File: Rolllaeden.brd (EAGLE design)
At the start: 160 x 100 mm, 62 parts, among them IC1 PCF8574P, IC2 PCF8574P, IC3 74HCT04N, IC4 74HCT08N, IC5 74HCT08N, J1 J7MM, J2 J7MM, T1 BC337-25, T2 BC337-25, T3 BC337-25, T4 BC337-25, T5 BC337-25, T6 BC337-25

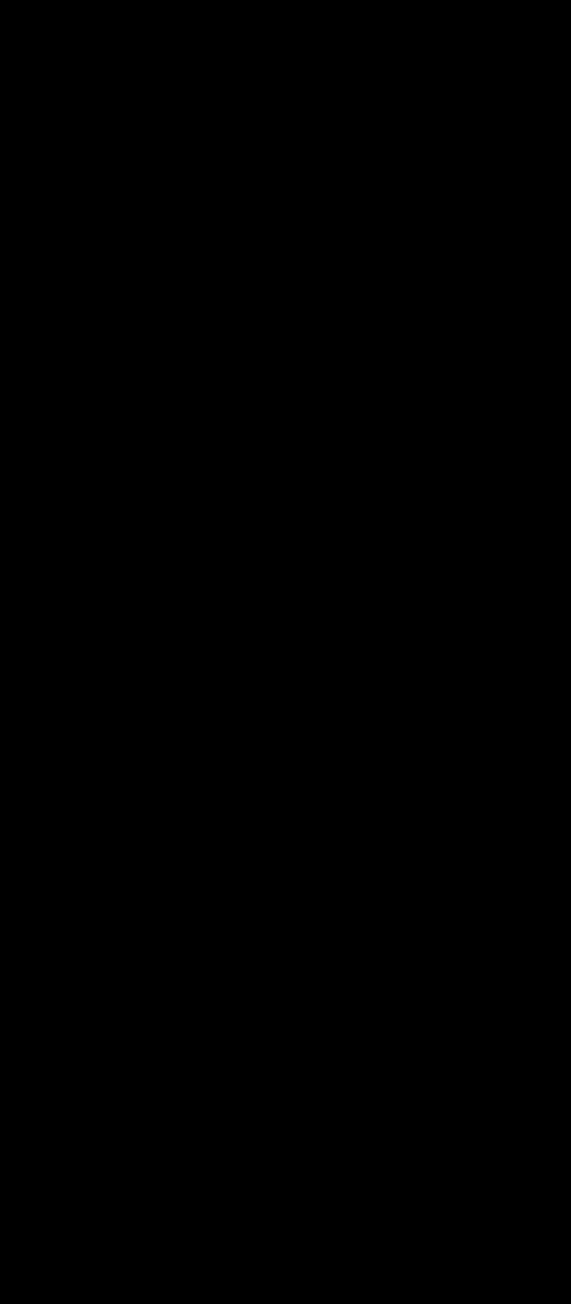
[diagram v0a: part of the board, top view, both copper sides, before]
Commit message: Pulldown-Widerstände zwichen Optokopplern und Logik-ICs hinzugefügt
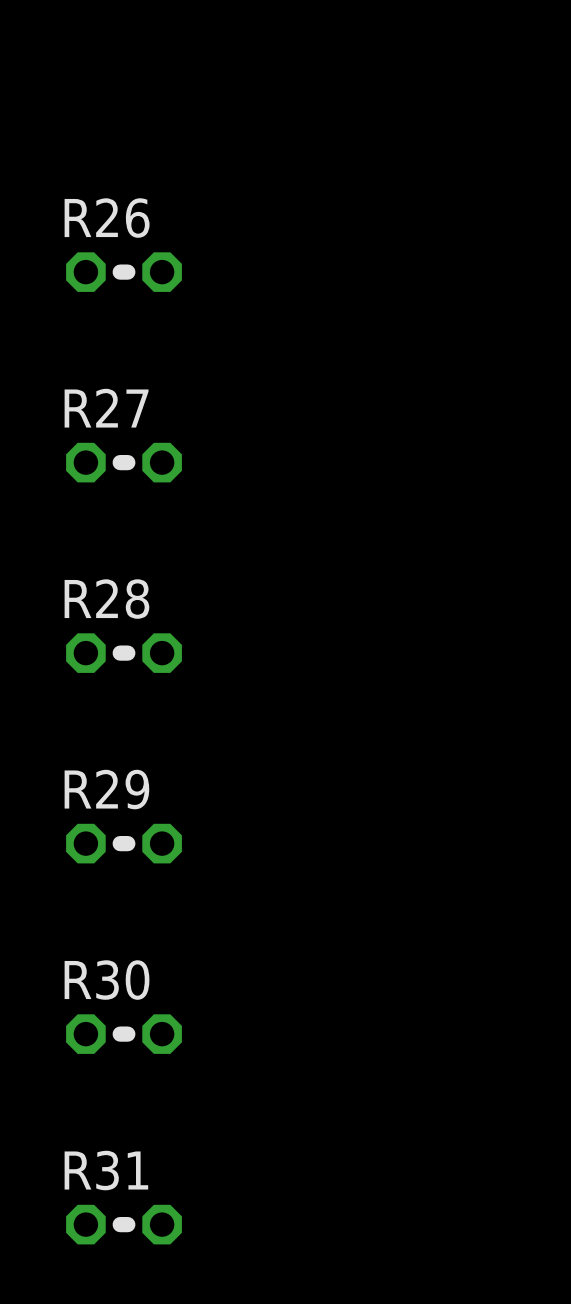
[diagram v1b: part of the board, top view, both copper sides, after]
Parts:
- added R26, R27, R28, R29, R30, R31: 10k, resistor:0204V
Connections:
- net GND: now also R26.1, R27.1, R28.1, R29.1, R30.1, R31.1
- net N$11: now also R30.2
- net N$22: now also R29.2
- net N$23: now also R28.2
- net N$34: now also R27.2
- net N$35: now also R26.2
- net N$4: now also R31.2
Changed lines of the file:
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@@
 <attribute name="OC_NEWARK" value="unknown" x="18.415" y="94.615" size="1.778" layer="27" display="off"/>
 </element>
+<element name="R26" library="resistor" package="0204V" value="10k" x="-11.43" y="-16.51"/>
+<element name="R27" library="resistor" package="0204V" value="10k" x="-11.43" y="-22.86"/>
+<element name="R28" library="resistor" package="0204V" value="10k" x="-11.43" y="-29.21"/>
+<element name="R29" library="resistor" package="0204V" value="10k" x="-11.43" y="-35.56"/>
+<element name="R30" library="resistor" package="0204V" value="10k" x="-11.43" y="-41.91"/>
+<element name="R31" library="resistor" package="0204V" value="10k" x="-11.43" y="-48.26"/>
 </elements>
 <signals>
@@
 <contactref element="SV3" pad="30T" route="any" routetag="1.30"/>
 <wire x1="5" y1="85.56" x2="9.36" y2="85.56" width="0.8128" layer="16"/>
+<contactref element="R26" pad="1"/>
+<contactref element="R27" pad="1"/>
+<contactref element="R28" pad="1"/>
+<contactref element="R29" pad="1"/>
+<contactref element="R30" pad="1"/>
+<contactref element="R31" pad="1"/>
+<wire x1="-12.7" y1="-41.91" x2="-12.7" y2="-48.26" width="0" layer="19" extent="1-1"/>
+<wire x1="-12.7" y1="-35.56" x2="-12.7" y2="-41.91" width="0" layer="19" extent="1-1"/>
+<wire x1="-12.7" y1="-29.21" x2="-12.7" y2="-35.56" width="0" layer="19" extent="1-1"/>
+<wire x1="-12.7" y1="-22.86" x2="-12.7" y2="-29.21" width="0" layer="19" extent="1-1"/>
+<wire x1="-12.7" y1="-16.51" x2="-12.7" y2="-22.86" width="0" layer="19" extent="1-1"/>
+<wire x1="46.99" y1="5.08" x2="-12.7" y2="-16.51" width="0" layer="19" extent="16-16"/>
 </signal>
 <signal name="N$1">
@@
 <wire x1="44.45" y1="54.61" x2="46.99" y2="57.15" width="0.4064" layer="1"/>
 <wire x1="46.99" y1="57.15" x2="49.53" y2="57.15" width="0.4064" layer="1"/>
+<contactref element="R31" pad="2"/>
+<wire x1="-10.16" y1="-48.26" x2="40.005" y2="37.465" width="0" layer="19" extent="1-1"/>
 </signal>
 <signal name="N$6">
@@
 <wire x1="50.8" y1="52.07" x2="49.53" y2="52.07" width="0.4064" layer="16"/>
 <wire x1="41.91" y1="39.37" x2="49.53" y2="39.37" width="0.4064" layer="1"/>
+<contactref element="R30" pad="2"/>
+<wire x1="-10.16" y1="-41.91" x2="41.91" y2="39.37" width="0" layer="19" extent="1-1"/>
 </signal>
 <signal name="N$16">
@@
 <wire x1="45.72" y1="27.94" x2="43.18" y2="30.48" width="0.4064" layer="1"/>
 <wire x1="43.18" y1="30.48" x2="41.91" y2="30.48" width="0.4064" layer="1"/>
+<contactref element="R29" pad="2"/>
+<wire x1="-10.16" y1="-35.56" x2="41.91" y2="30.48" width="0" layer="19" extent="1-1"/>
 </signal>
 <signal name="N$23">
@@
 <wire x1="39.37" y1="29.845" x2="40.005" y2="29.21" width="0.4064" layer="1"/>
 <wire x1="40.005" y1="29.21" x2="42.545" y2="29.21" width="0.4064" layer="1"/>
+<contactref element="R28" pad="2"/>
+<wire x1="-10.16" y1="-29.21" x2="41.91" y2="21.59" width="0" layer="19" extent="1-1"/>
 </signal>
 <signal name="N$25">
@@
 <wire x1="54.61" y1="10.16" x2="55.88" y2="8.89" width="0.4064" layer="16"/>
 <wire x1="55.88" y1="8.89" x2="57.15" y2="8.89" width="0.4064" layer="16"/>
+<contactref element="R27" pad="2"/>
+<wire x1="-10.16" y1="-22.86" x2="41.91" y2="12.7" width="0" layer="19" extent="1-1"/>
 </signal>
 <signal name="N$35">
@@
 <wire x1="44.45" y1="5.08" x2="43.18" y2="3.81" width="0.4064" layer="1"/>
 <wire x1="43.18" y1="3.81" x2="41.91" y2="3.81" width="0.4064" layer="1"/>
+<contactref element="R26" pad="2"/>
+<wire x1="-10.16" y1="-16.51" x2="41.91" y2="3.81" width="0" layer="19" extent="1-1"/>
 </signal>
 <signal name="N$36">

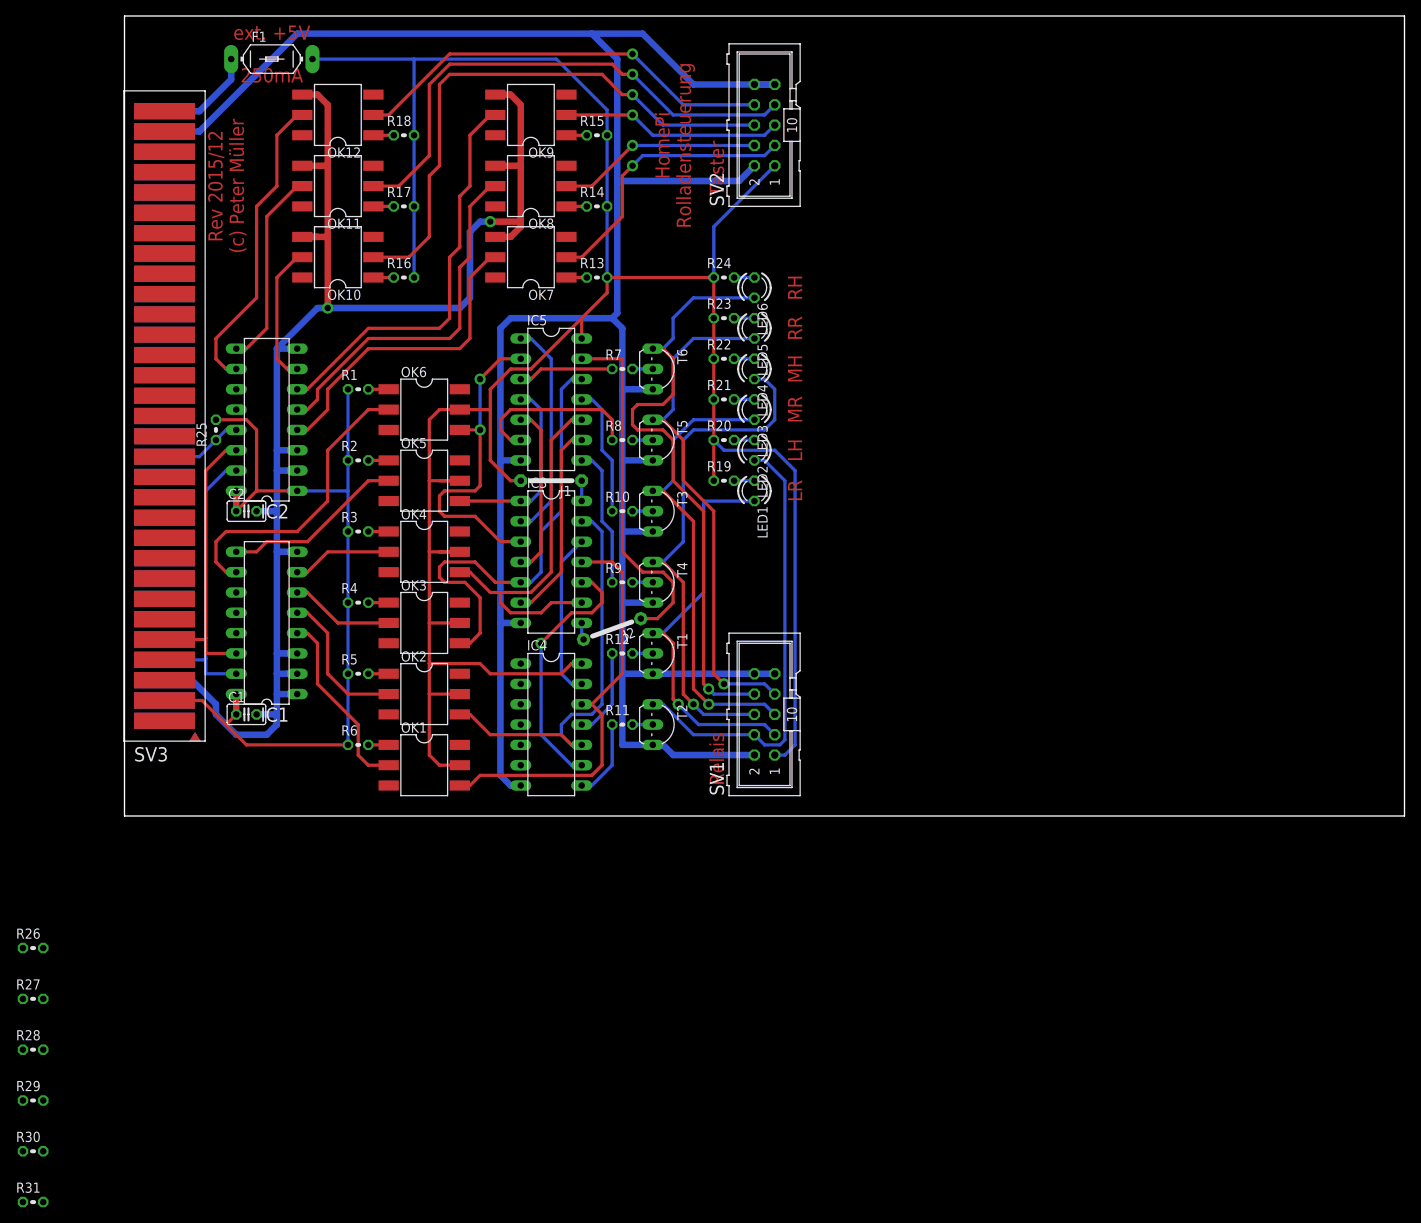
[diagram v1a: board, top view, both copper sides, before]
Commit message: Schaltpläne aufgehübscht zur Veröffentlichung
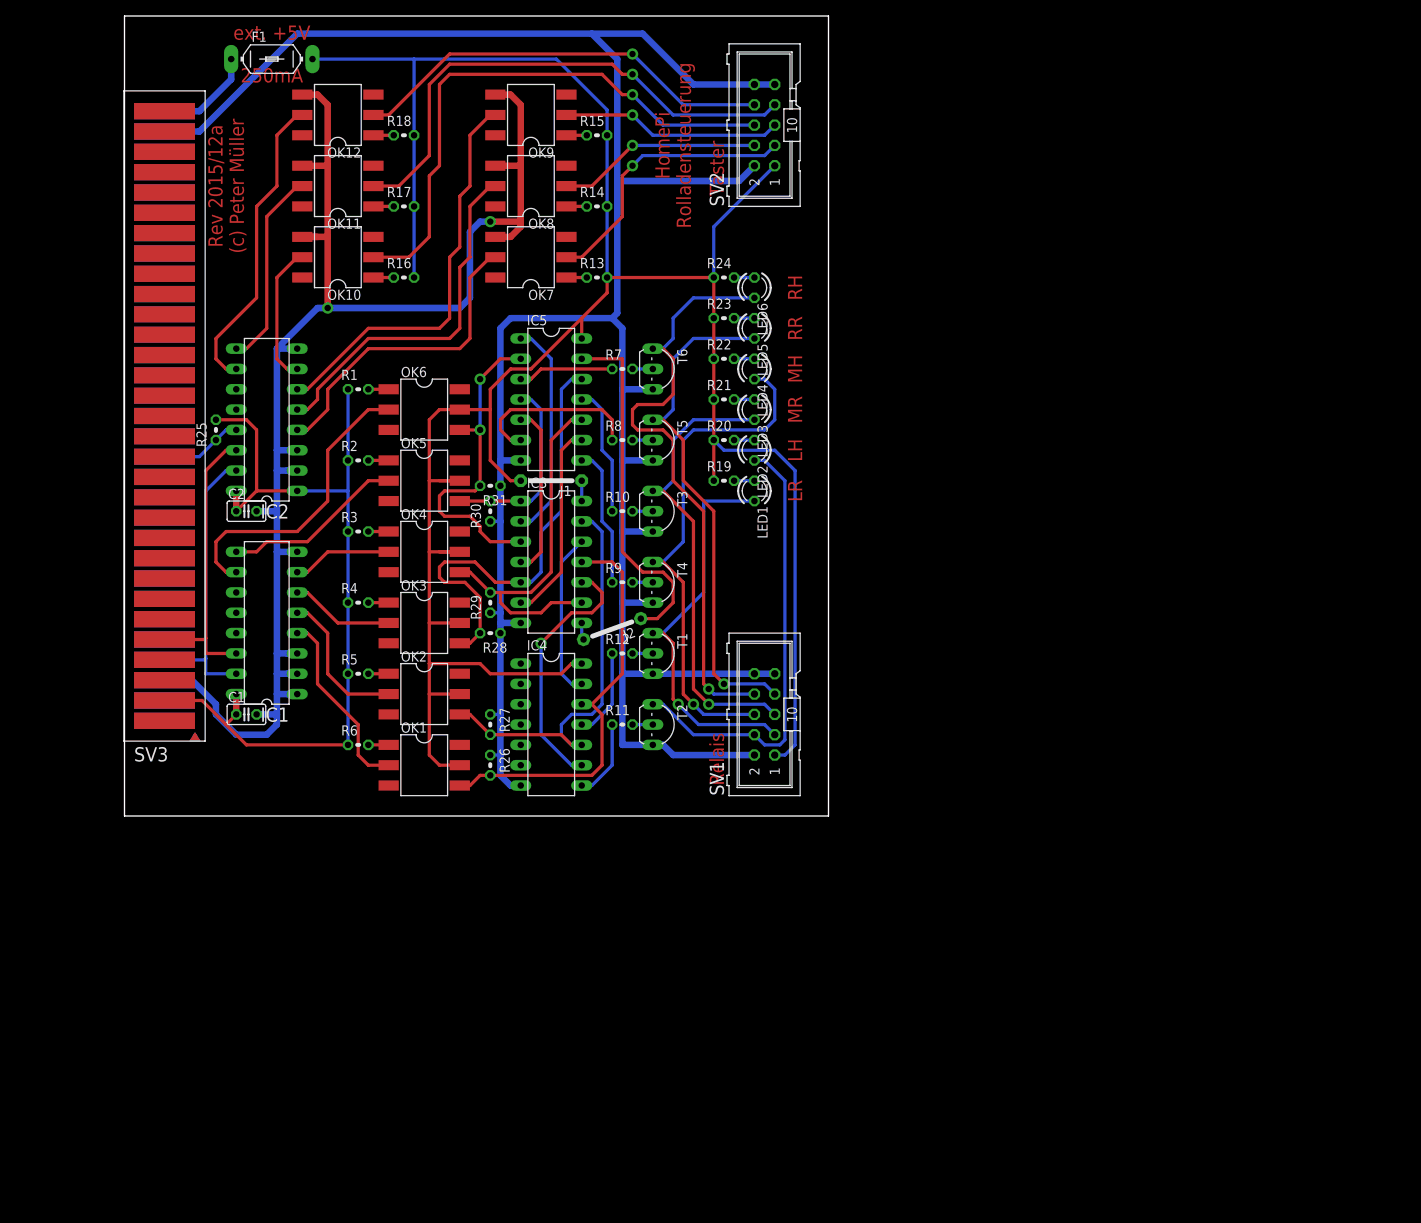
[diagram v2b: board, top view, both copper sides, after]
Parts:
- moved R31 106.2 mm to (45.7, 41.3), turned to 180 degrees
- moved R30 98.3 mm to (45.7, 38.1), turned to 90 degrees
- moved R29 84.5 mm to (45.7, 26.7), turned to 90 degrees
- moved R28 77.3 mm to (45.7, 22.9), turned to 180 degrees
- moved R27 66.6 mm to (45.7, 11.4), turned to 270 degrees
- moved R26 61.6 mm to (45.7, 6.35), turned to 270 degrees
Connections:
- net N$16 renamed SIG_RR
- net N$32 renamed SIG_MH
- net N$33 renamed SIG_MR
- net N$36 renamed SIG_LH
- net N$37 renamed SIG_LR
- net N$47 renamed T_LR
- net N$48 renamed T_LH
- net N$50 renamed T_MR
- net N$51 renamed T_MH
- net N$56 renamed T_RR
- net N$57 renamed T_RH
- net N$99 renamed SIG_RH
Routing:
- net GND: track 325.3 -> 327.8 mm
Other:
- board size 160 x 100 mm -> 88 x 100 mm
- board text added: "Rev 2015/12a (c) Peter Müller"
- board text removed: "Rev 2015/12 (c) Peter Müller"
